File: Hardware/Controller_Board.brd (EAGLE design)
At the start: 100 x 100 mm, 29 parts, among them Q7 3.6864MHz, U1 ATMEGA328P-PU, U2 LM1086CT-3.3

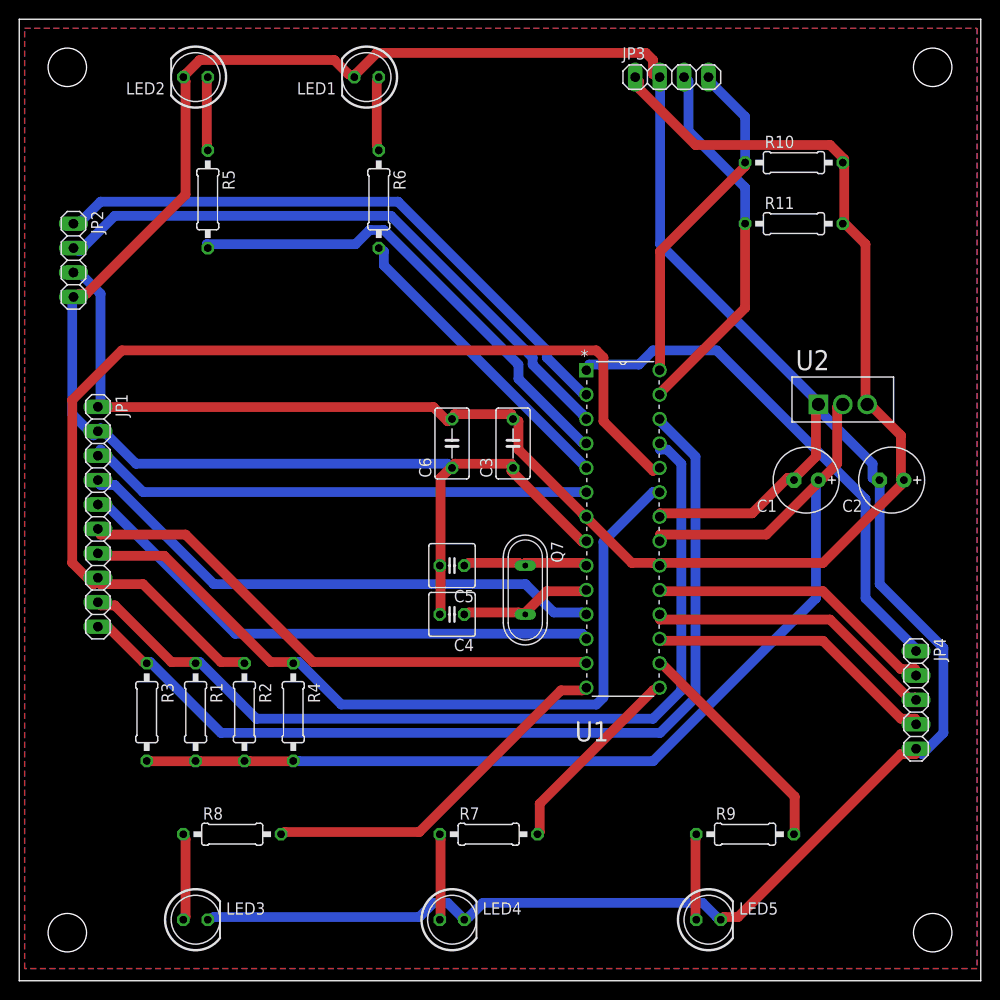
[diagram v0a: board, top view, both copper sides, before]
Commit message: Added +3.3V and a GPIO to the controller board extension connector.
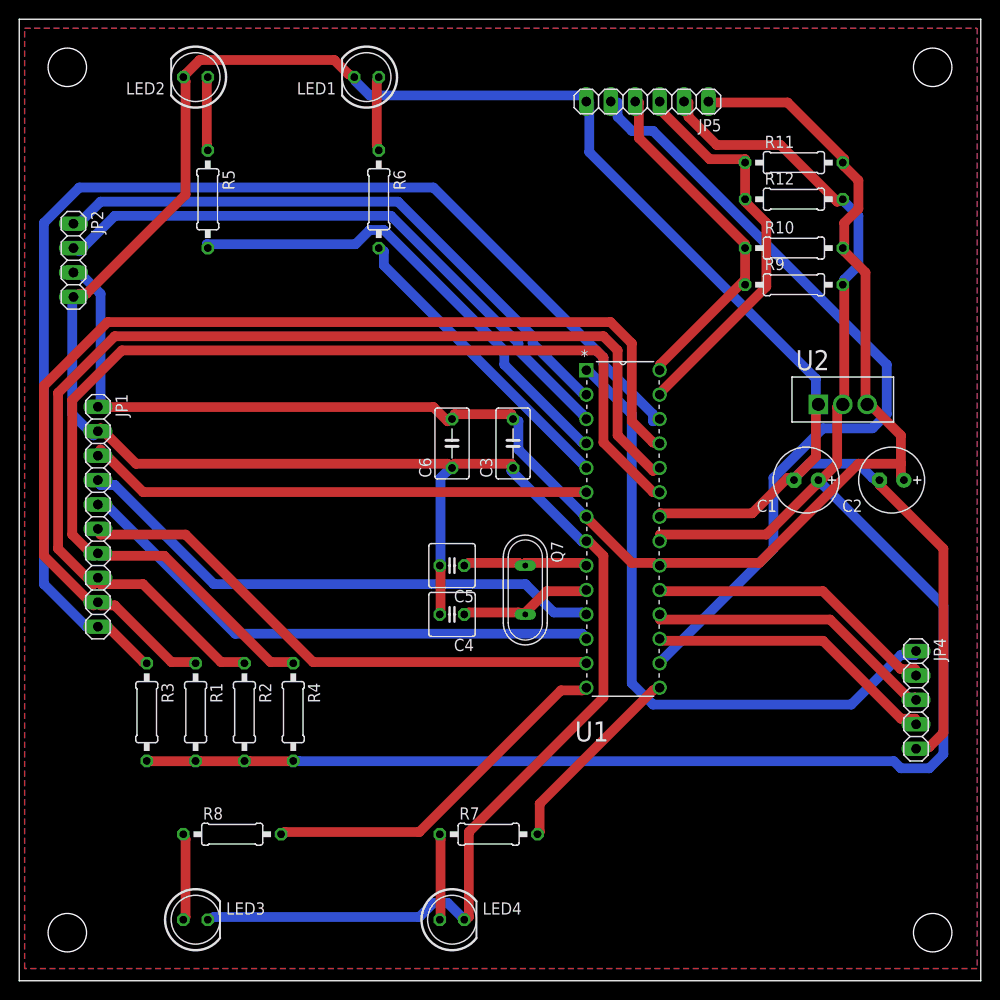
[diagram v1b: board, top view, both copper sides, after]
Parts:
- removed JP3: I2C temperature sensor, pinhead:1X04
- removed LED5: Mixing valve, led:LED5MM
- added JP5: Extension, pinhead:1X06
- added R12: 1K, resistor:0207/10
- R9: value 330 -> 1K
- moved R9 57.4 mm to (115.6, 72.4)
- moved R10 8.89 mm to (115.6, 76.2)
- moved R11 6.35 mm to (115.6, 85.1)
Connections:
- removed net N$28: R9.2, U1.16
- net +3V3: now also JP5.2, R12.2, R9.2
- net GND: now also JP5.6; no longer JP3.2, LED5.K
- net N$20: now also JP5.3, R12.1; no longer JP3.3
- net N$23: now also JP5.4, R9.1; no longer JP3.4
- net N$26: now also JP5.5, U1.16; no longer LED5.A, R9.1
- net VCC: now also JP5.1; no longer JP3.1
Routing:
- net N$26: track 8.91 -> 84.7 mm
- net +3V3: track 117.7 -> 190.8 mm
- net N$4: track 83.6 -> 117.2 mm
- net N$1: track 98.8 -> 128.2 mm
- net N$28: track 23.9 -> 0.00 mm
- net N$2: track 94.0 -> 115.0 mm
- net GND: track 364.3 -> 344.9 mm
- net N$19: track 54.4 -> 67.5 mm
- net VCC: track 174.5 -> 166.8 mm
- net N$3: track 112.3 -> 117.3 mm
- net N$20: track 39.4 -> 41.8 mm
- net N$23: track 35.7 -> 37.0 mm
- added copper zone on layer 16, net N$16
- added copper zone on layer 1, net N$28
- removed copper zone on layer 1, net N$16
- removed copper zone on layer 16, net N$30
